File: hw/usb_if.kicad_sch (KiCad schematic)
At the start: 13 parts, among them J1 USB_C_Receptacle_USB2.0, U16 USB3343

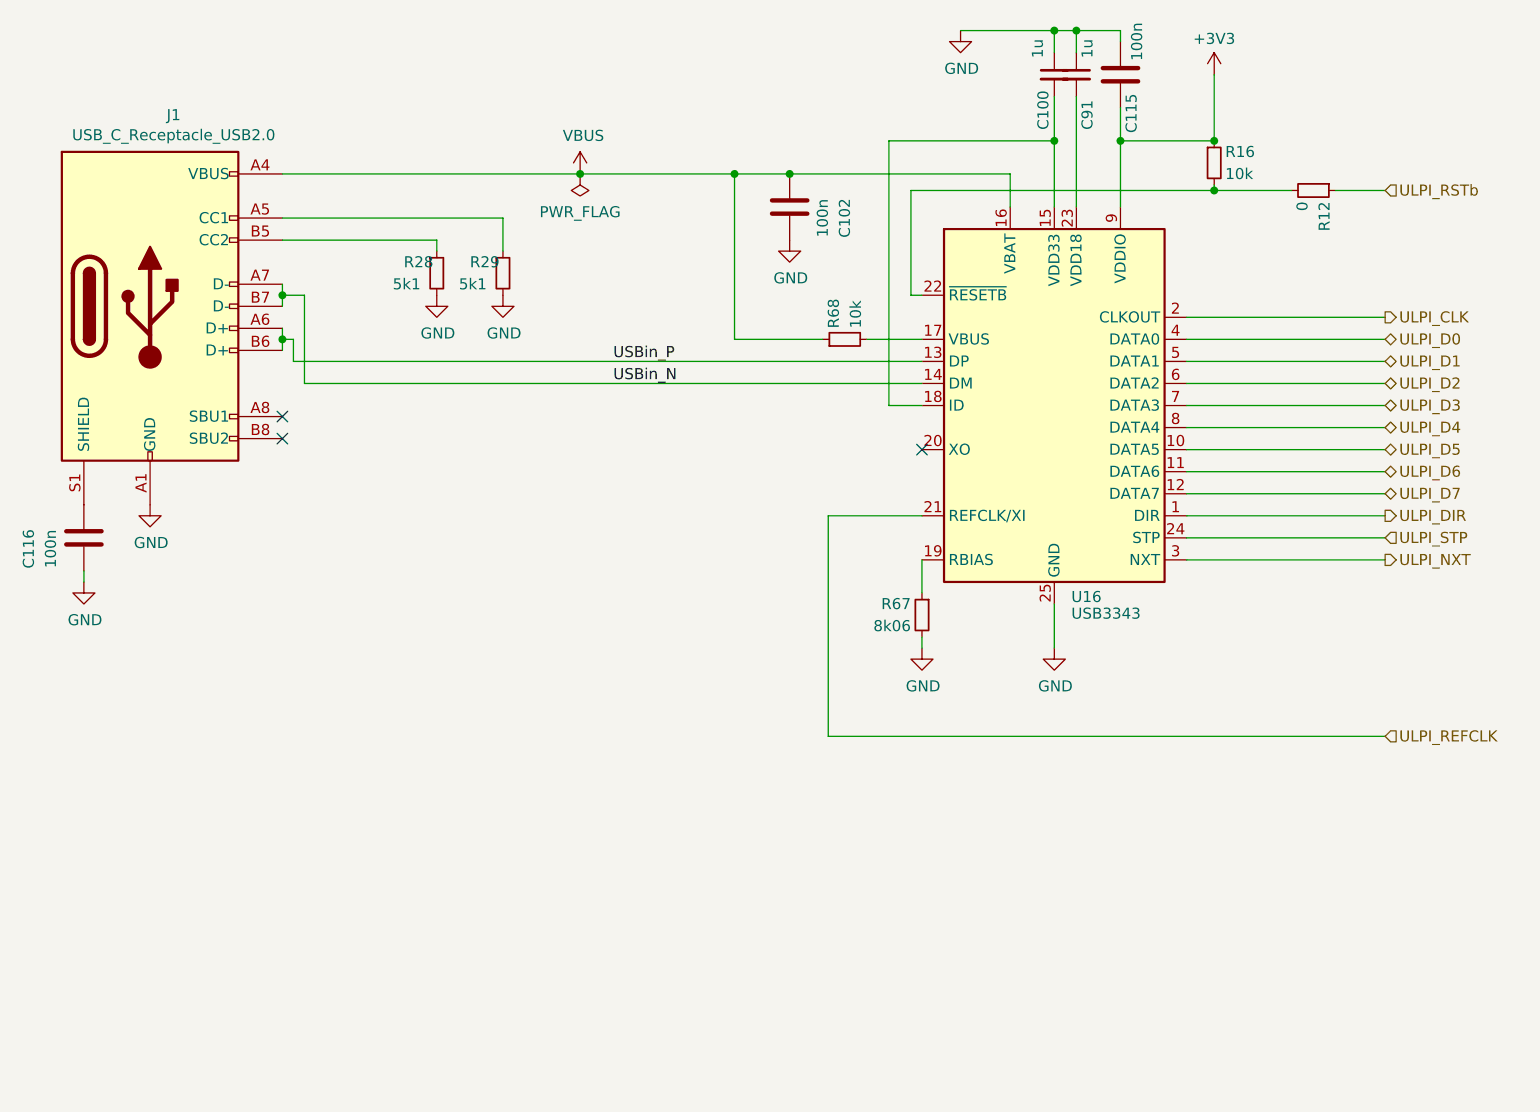
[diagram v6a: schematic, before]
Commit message: consolidated components to simplify BOM
(nothing actually changed but the symbols representing identical
components are now identical -> no more multiple BOM entries for
the same type of component).
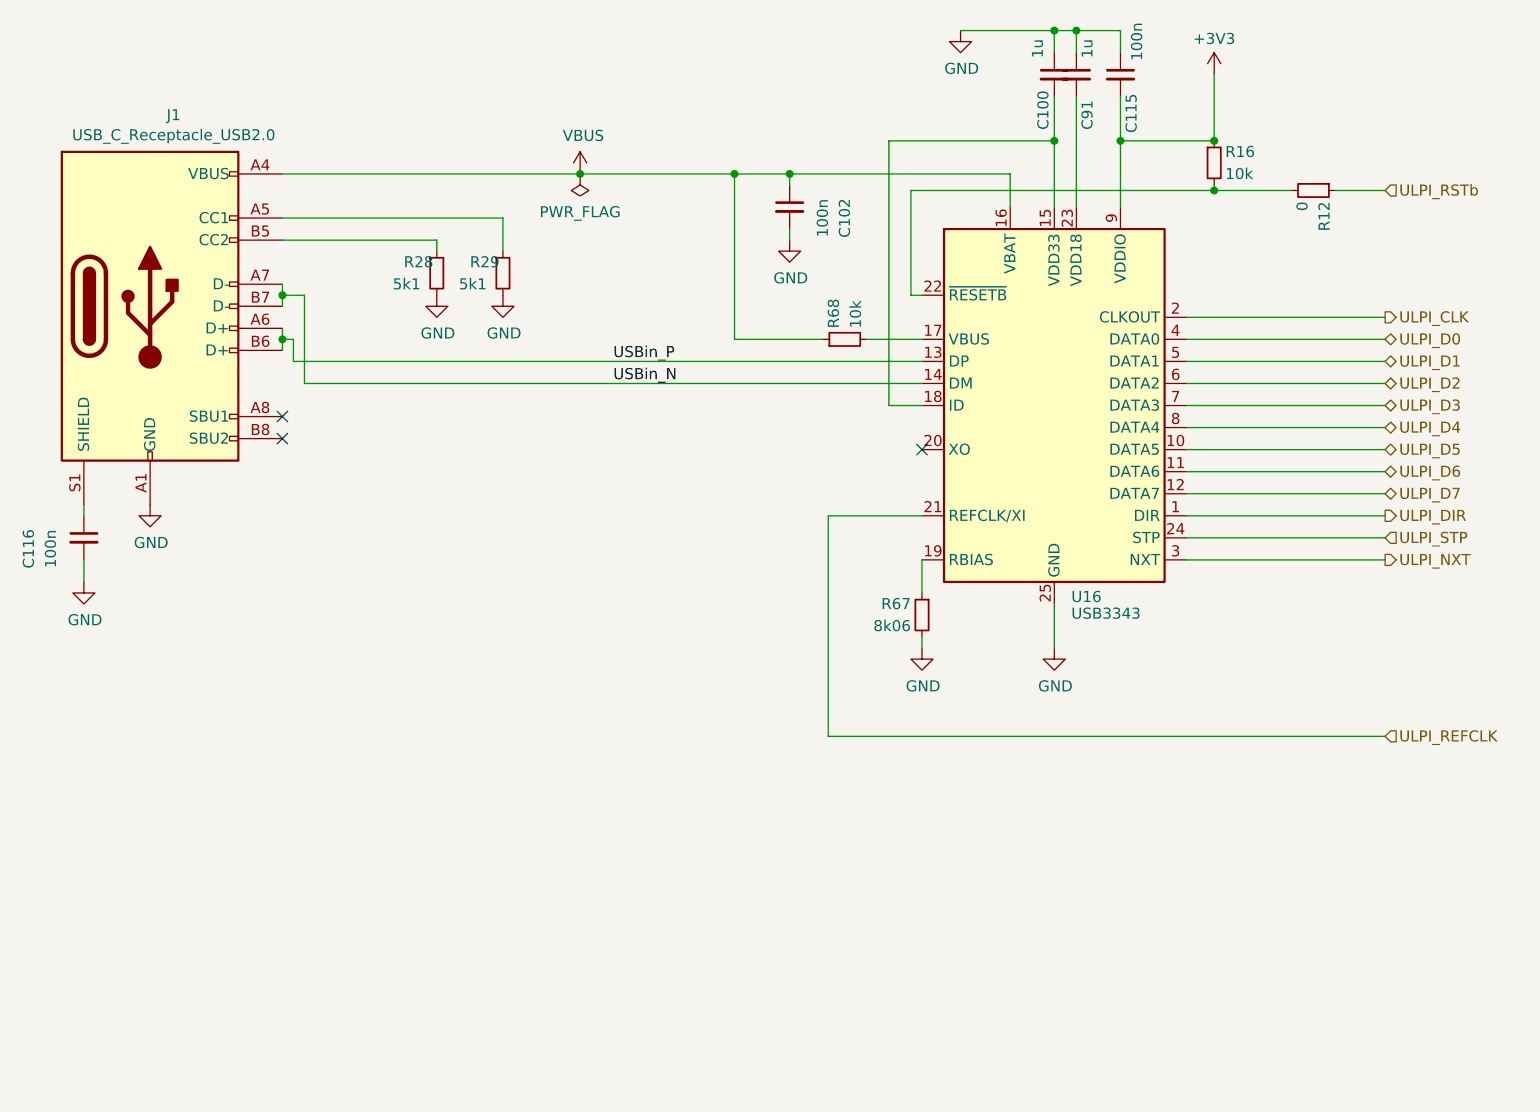
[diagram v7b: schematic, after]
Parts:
- C102, C115, C116: symbol fmc:100nF_603 -> Device:C_Small; Manufacturer (none) -> Samsung; Part (none) -> CL10B104KB8NFN
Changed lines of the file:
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@@
 (kicad_sch (version 20230121) (generator eeschema)
   (paper "A4")
+  (junction (at 127 58.42) (diameter 0) (color 0 0 0 0)
+  )
   (junction (at 68.58 72.39) (diameter 0) (color 0 0 0 0)
   )
@@
   )
   (junction (at 102.87 58.42) (diameter 0) (color 0 0 0 0)
-  )
-  (junction (at 127 58.42) (diameter 0) (color 0 0 0 0)
   )
   (junction (at 165.1 54.61) (diameter 0) (color 0 0 0 0)
@@
     (stroke (width 0) (type default))
   )
+  (wire (pts (xy 127 58.42) (xy 152.4 58.42))
+    (stroke (width 0) (type default))
+  )
   (wire (pts (xy 172.72 90.17) (xy 195.58 90.17))
     (stroke (width 0) (type default))
@@
     (stroke (width 0) (type default))
   )
-  (wire (pts (xy 45.72 104.14) (xy 45.72 105.41))
+  (wire (pts (xy 45.72 102.87) (xy 45.72 105.41))
     (stroke (width 0) (type default))
   )
@@
     (stroke (width 0) (type default))
   )
+  (wire (pts (xy 127 64.77) (xy 127 66.04))
+    (stroke (width 0) (type default))
+  )
   (wire (pts (xy 69.85 80.01) (xy 142.24 80.01))
     (stroke (width 0) (type default))
@@
     (stroke (width 0) (type default))
   )
+  (wire (pts (xy 45.72 96.52) (xy 45.72 97.79))
+    (stroke (width 0) (type default))
+  )
   (wire (pts (xy 68.58 66.04) (xy 86.36 66.04))
     (stroke (width 0) (type default))
@@
     (stroke (width 0) (type default))
   )
-  (wire (pts (xy 152.4 58.42) (xy 127 58.42))
+  (wire (pts (xy 120.65 58.42) (xy 127 58.42))
     (stroke (width 0) (type default))
   )
@@
     (stroke (width 0) (type default))
   )
-  (wire (pts (xy 165.1 50.8) (xy 165.1 54.61))
+  (wire (pts (xy 165.1 49.53) (xy 165.1 54.61))
     (stroke (width 0) (type default))
   )
@@
     (stroke (width 0) (type default))
   )
+  (wire (pts (xy 127 58.42) (xy 127 59.69))
+    (stroke (width 0) (type default))
+  )
   (wire (pts (xy 142.24 102.87) (xy 142.24 106.68))
     (stroke (width 0) (type default))
@@
     (stroke (width 0) (type default))
   )
-  (wire (pts (xy 165.1 43.18) (xy 165.1 41.91))
+  (wire (pts (xy 165.1 41.91) (xy 165.1 44.45))
     (stroke (width 0) (type default))
   )
@@
   )
   (wire (pts (xy 157.48 107.95) (xy 157.48 113.03))
-    (stroke (width 0) (type default))
-  )
-  (wire (pts (xy 127 58.42) (xy 120.65 58.42))
     (stroke (width 0) (type default))
   )
@@
     )
   )
-  (symbol (lib_id "fmc:100nF_603") (at 45.72 100.33 0) (mirror y) (unit 1)
+  (symbol (lib_id "Device:C_Small") (at 45.72 100.33 0) (mirror y) (unit 1)
     (in_bom yes) (on_board yes) (dnp no)
     (property "Reference" "C116" (at 39.37 101.6 90)
@@
       (effects (font (size 1.27 1.27)))
     )
-    (property "Footprint" "Capacitor_SMD:C_0603_1608Metric" (at 44.7548 104.14 0)
+    (property "Footprint" "Capacitor_SMD:C_0603_1608Metric" (at 45.72 100.33 0)
       (effects (font (size 1.27 1.27)) hide)
     )
@@
       (effects (font (size 1.27 1.27)) hide)
     )
-    (property "Part" "" (at 42.545 95.25 0)
-      (effects (font (size 1.27 1.27)) hide)
-    )
-    (property "Manufacturer" "" (at 40.005 92.71 0)
+    (property "Part" "CL10B104KB8NFN" (at 42.545 95.25 0)
+      (effects (font (size 1.27 1.27)) hide)
+    )
+    (property "Manufacturer" "Samsung" (at 40.005 92.71 0)
       (effects (font (size 1.27 1.27)) hide)
     )
@@
     )
   )
-  (symbol (lib_id "fmc:100nF_603") (at 165.1 46.99 0) (unit 1)
+  (symbol (lib_id "Device:C_Small") (at 165.1 46.99 0) (unit 1)
     (in_bom yes) (on_board yes) (dnp no)
     (property "Reference" "C115" (at 166.37 51.435 90)
@@
       (effects (font (size 1.27 1.27)))
     )
-    (property "Footprint" "Capacitor_SMD:C_0603_1608Metric" (at 166.0652 50.8 0)
+    (property "Footprint" "Capacitor_SMD:C_0603_1608Metric" (at 165.1 46.99 0)
       (effects (font (size 1.27 1.27)) hide)
     )
@@
       (effects (font (size 1.27 1.27)) hide)
     )
-    (property "Part" "" (at 168.275 41.91 0)
-      (effects (font (size 1.27 1.27)) hide)
-    )
-    (property "Manufacturer" "" (at 170.815 39.37 0)
+    (property "Part" "CL10B104KB8NFN" (at 168.275 41.91 0)
+      (effects (font (size 1.27 1.27)) hide)
+    )
+    (property "Manufacturer" "Samsung" (at 170.815 39.37 0)
       (effects (font (size 1.27 1.27)) hide)
     )
@@
     )
   )
-  (symbol (lib_id "fmc:100nF_603") (at 127 62.23 0) (unit 1)
+  (symbol (lib_id "Device:C_Small") (at 127 62.23 0) (unit 1)
     (in_bom yes) (on_board yes) (dnp no)
     (property "Reference" "C102" (at 133.35 63.5 90)
@@
       (effects (font (size 1.27 1.27)))
     )
-    (property "Footprint" "Capacitor_SMD:C_0603_1608Metric" (at 127.9652 66.04 0)
+    (property "Footprint" "Capacitor_SMD:C_0603_1608Metric" (at 127 62.23 0)
       (effects (font (size 1.27 1.27)) hide)
     )
@@
       (effects (font (size 1.27 1.27)) hide)
     )
-    (property "Part" "" (at 130.175 57.15 0)
-      (effects (font (size 1.27 1.27)) hide)
-    )
-    (property "Manufacturer" "" (at 132.715 54.61 0)
-      (effects (font (size 1.27 1.27)) hide)
-    )
+    (property "Part" "CL10B104KB8NFN" (at 130.175 57.15 0)
+      (effects (font (size 1.27 1.27)) hide)
+    )
+    (property "Manufacturer" "Samsung" (at 132.715 54.61 0)
+      (effects (font (size 1.27 1.27)) hide)
+    )

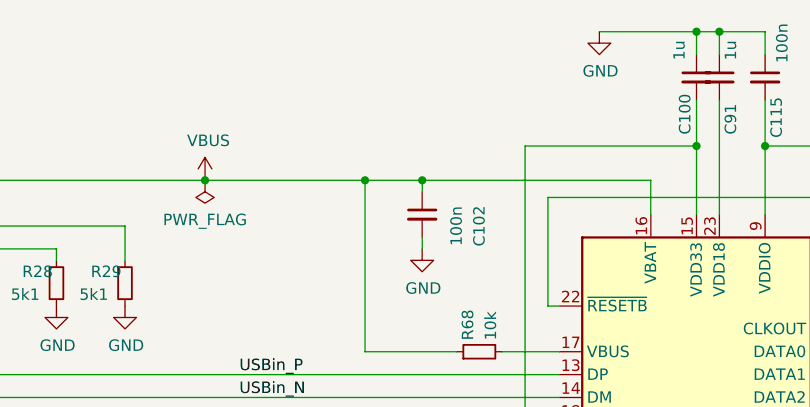
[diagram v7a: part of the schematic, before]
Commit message: [hw] added reset generator; removed 5V fill from FE area!
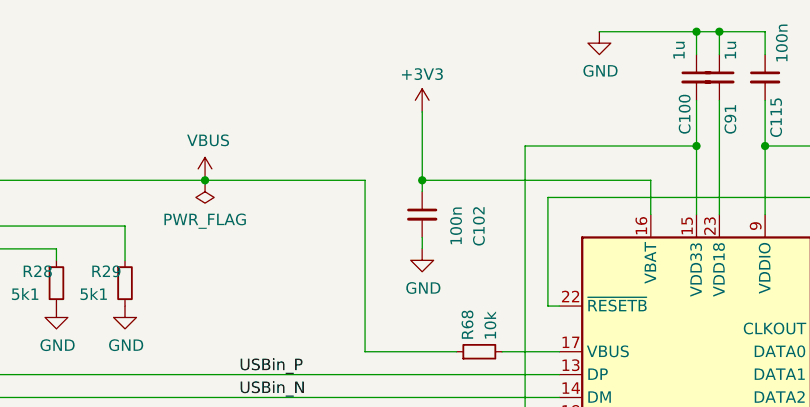
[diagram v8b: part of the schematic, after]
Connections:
- net +3V3: now also C102.1, U16.16 (VBAT)
- net VBUS: no longer C102.1, U16.16 (VBAT)
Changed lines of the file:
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@@
 (kicad_sch (version 20230121) (generator eeschema)
   (paper "A4")
+  (junction (at 68.58 72.39) (diameter 0) (color 0 0 0 0)
+  )
+  (junction (at 175.895 54.61) (diameter 0) (color 0 0 0 0)
+  )
+  (junction (at 102.87 58.42) (diameter 0) (color 0 0 0 0)
+  )
   (junction (at 127 58.42) (diameter 0) (color 0 0 0 0)
-  )
-  (junction (at 68.58 72.39) (diameter 0) (color 0 0 0 0)
-  )
-  (junction (at 120.65 58.42) (diameter 0) (color 0 0 0 0)
-  )
-  (junction (at 175.895 54.61) (diameter 0) (color 0 0 0 0)
-  )
-  (junction (at 102.87 58.42) (diameter 0) (color 0 0 0 0)
   )
   (junction (at 165.1 54.61) (diameter 0) (color 0 0 0 0)
@@
     (stroke (width 0) (type default))
   )
+  (wire (pts (xy 127 58.42) (xy 127 50.8))
+    (stroke (width 0) (type default))
+  )
   (wire (pts (xy 45.72 96.52) (xy 45.72 97.79))
     (stroke (width 0) (type default))
@@
   )
   (wire (pts (xy 172.72 82.55) (xy 195.58 82.55))
-    (stroke (width 0) (type default))
-  )
-  (wire (pts (xy 120.65 58.42) (xy 127 58.42))
     (stroke (width 0) (type default))
   )
@@
         )
       )
+    )
+  )
+  (symbol (lib_id "power:+3V3") (at 127 50.8 0) (unit 1)
+    (in_bom yes) (on_board yes) (dnp no) (fields_autoplaced)
+    (property "Reference" "#PWR0131" (at 127 54.61 0)
+      (effects (font (size 1.27 1.27)) hide)
+    )
+    (property "Value" "+3V3" (at 127 46.6669 0)
+      (effects (font (size 1.27 1.27)))
+    )
+    (property "Footprint" "" (at 127 50.8 0)
+      (effects (font (size 1.27 1.27)) hide)
+    )
+    (property "Datasheet" "" (at 127 50.8 0)
+      (effects (font (size 1.27 1.27)) hide)
+    )
+    (pin "1")
+    (instances
+      (project "usbadc"
+        (path "/7c8a1f8d-8834-4c9b-aaae-1f231e9b09a1/5598a6a2-be47-454c-8f97-749ceb56c3dc"
+          (reference "#PWR0131") (unit 1)
+        )
+      )
